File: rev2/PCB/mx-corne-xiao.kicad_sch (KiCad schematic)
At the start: 70 parts, among them J1 OLED, SW1 SW_PUSH, SW10 SW_PUSH, SW11 SW_PUSH, SW12 SW_PUSH, SW13 SW_PUSH, SW14 SW_PUSH, SW15 SW_PUSH, SW16 SW_PUSH, SW17 SW_PUSH, SW18 SW_PUSH, SW19 SW_PUSH, SW2 SW_PUSH, SW20 SW_PUSH, SW21 SW_PUSH, SW3 SW_PUSH, SW4 SW_PUSH, SW44 RotaryEncoder_Switch, SW5 SW_PUSH, SW6 SW_PUSH, SW7 SW_PUSH, SW8 SW_PUSH, SW9 SW_PUSH, U1 xiao-ble

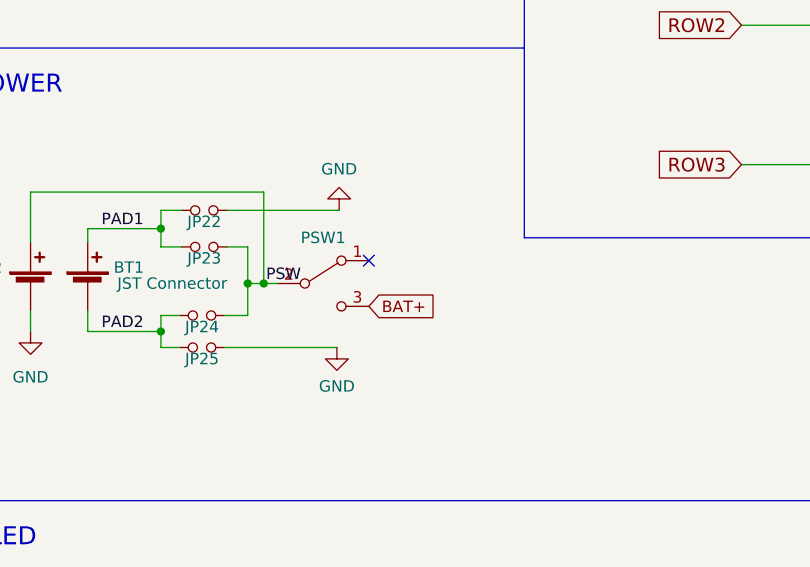
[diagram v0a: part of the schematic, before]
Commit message: added teardrops and increased via diameter to match some vendor's capabilites
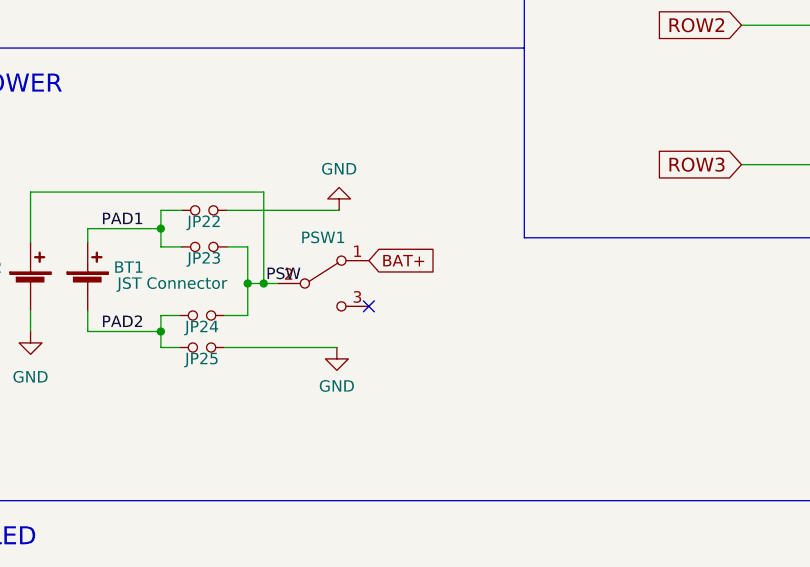
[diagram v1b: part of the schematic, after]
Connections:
- net BAT+: now also PSW1.1 (A); no longer PSW1.3 (C)
